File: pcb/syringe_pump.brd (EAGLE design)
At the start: 59.4 x 56.3 mm, 20 parts, among them J1 PJ-102AH, J2 SJ-435107RS, P1 OSTTE020104, P2 OSTTE020104, P3 OSTTE020104, P4 OSTTE020104, Q1 2N7000, Q2 2N7000, SW1 PEC11R-4215F-S0024, U1 R-785.0-0.5

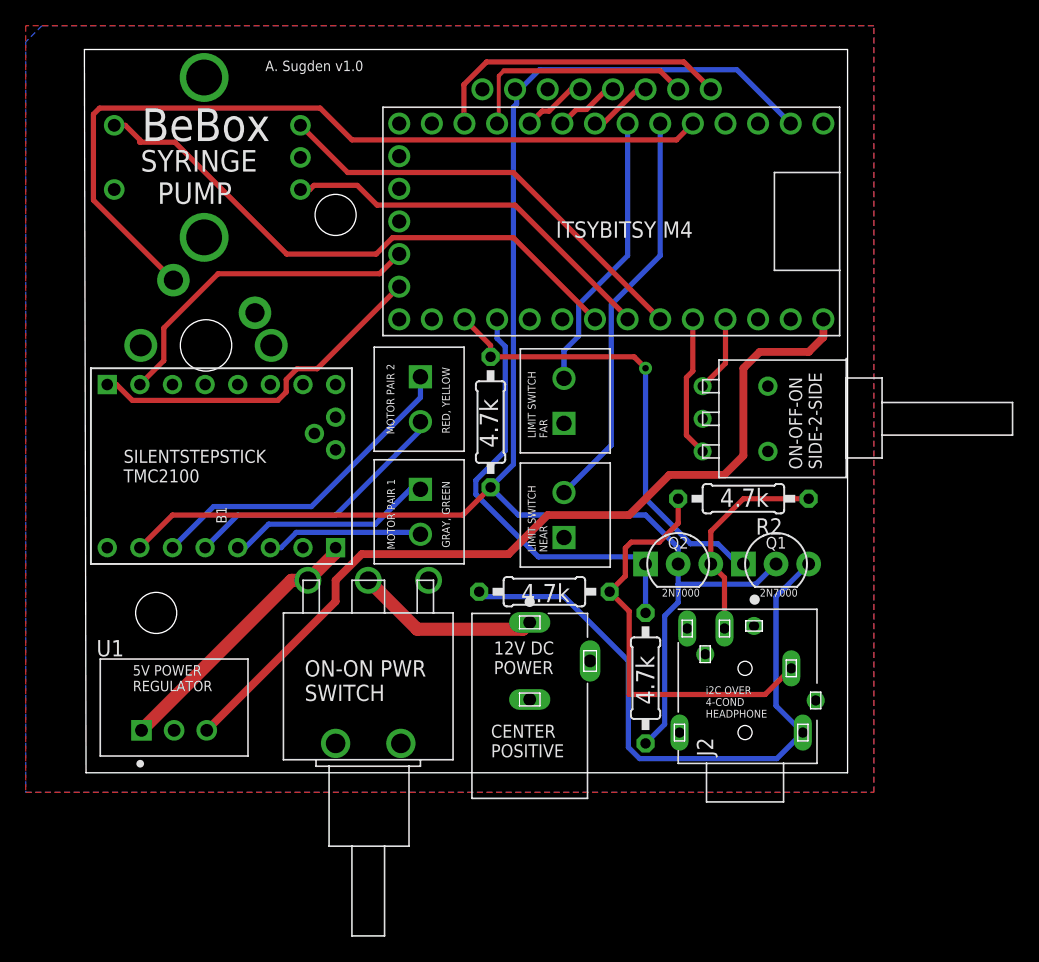
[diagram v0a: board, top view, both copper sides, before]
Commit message: Updated spacing of syringe pump and added copy of encoder library due to version issues.
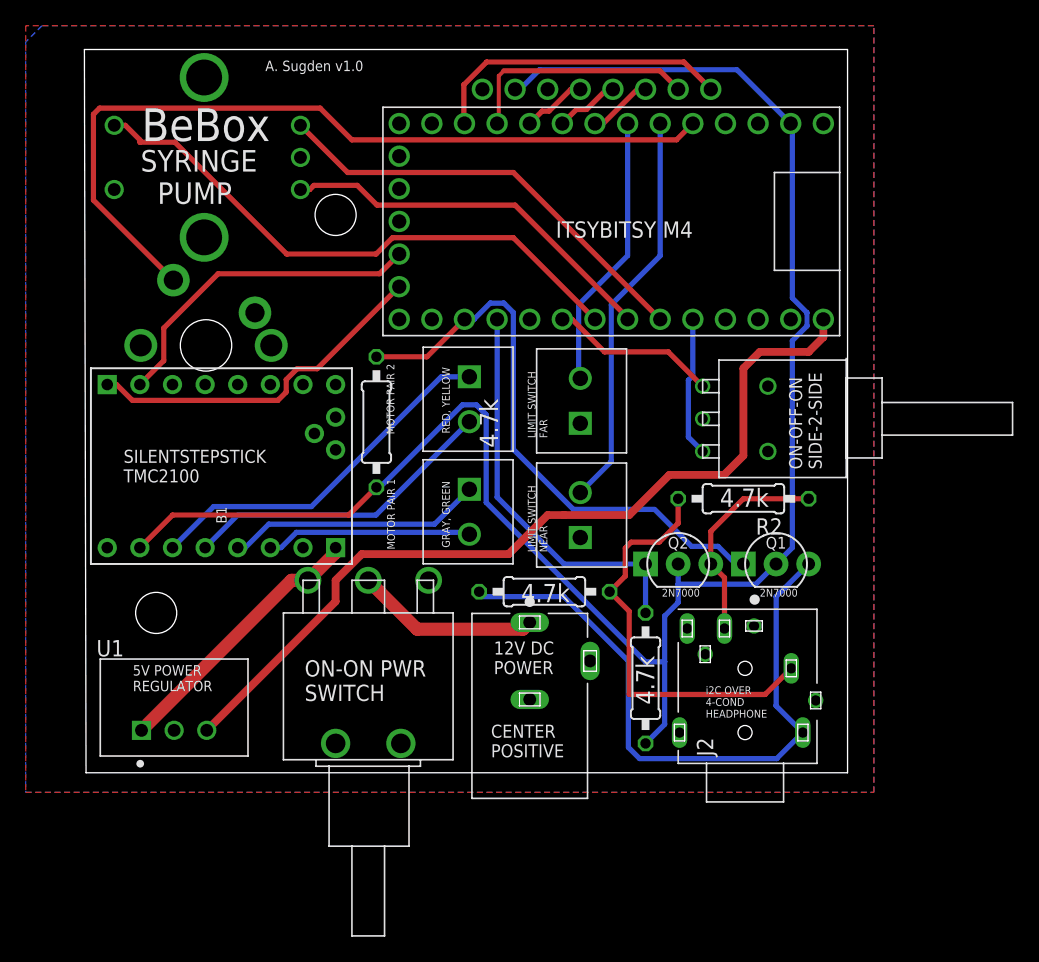
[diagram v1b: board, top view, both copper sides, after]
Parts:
- moved R8 8.89 mm to (26.0, 27.6)
- moved P1 3.81 mm to (33.3, 29.3)
- moved P2 3.81 mm to (33.3, 20.6)
- moved P3 1.27 mm to (41.9, 20.3)
- moved P4 1.27 mm to (41.9, 29.2)
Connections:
- net N$22: now also U$1.D7; no longer U$1.D13
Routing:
- net 3.3V: track 126.3 -> 140.7 mm
- net N$1: track 36.1 -> 45.0 mm, vias 1 -> 0
- net N$22: track 5.94 -> 13.1 mm
- net N$7: track 16.1 -> 19.9 mm
- net N$6: track 12.2 -> 16.0 mm
- net N$9: track 21.2 -> 24.6 mm
- net N$8: track 25.8 -> 28.6 mm
- net N$5: track 34.1 -> 31.4 mm
- net N$19: track 31.8 -> 31.3 mm
